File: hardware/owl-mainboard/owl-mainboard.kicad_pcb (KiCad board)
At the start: 4 copper layers, 61.8 x 79.8 mm, 107 parts, among them J101 Battery +, -, J201 USB-C, J202 EXP: GND, 3V3, A, B, J301 AMOLED FPC, J302 LRA, J303 DOCK: GND, VBUS, DET, GND, SW201 Ear left, SW202 Ear right, SW203 Beak, U101 BQ24073RGTR, U102 MAX17048G+T10, U103 TPS63802DLAR, U104 TPS22917DBVR, U201 ESP32-S3-WROOM-1-N16R8, U202 USBLC6-2SC6, U301 DRV2605LDGSR, U302 TMAG5273A2QDBVR, U303 LIS2DW12TR, U304 OPT3001DNPR, Y201 32.768kHz 12.5pF

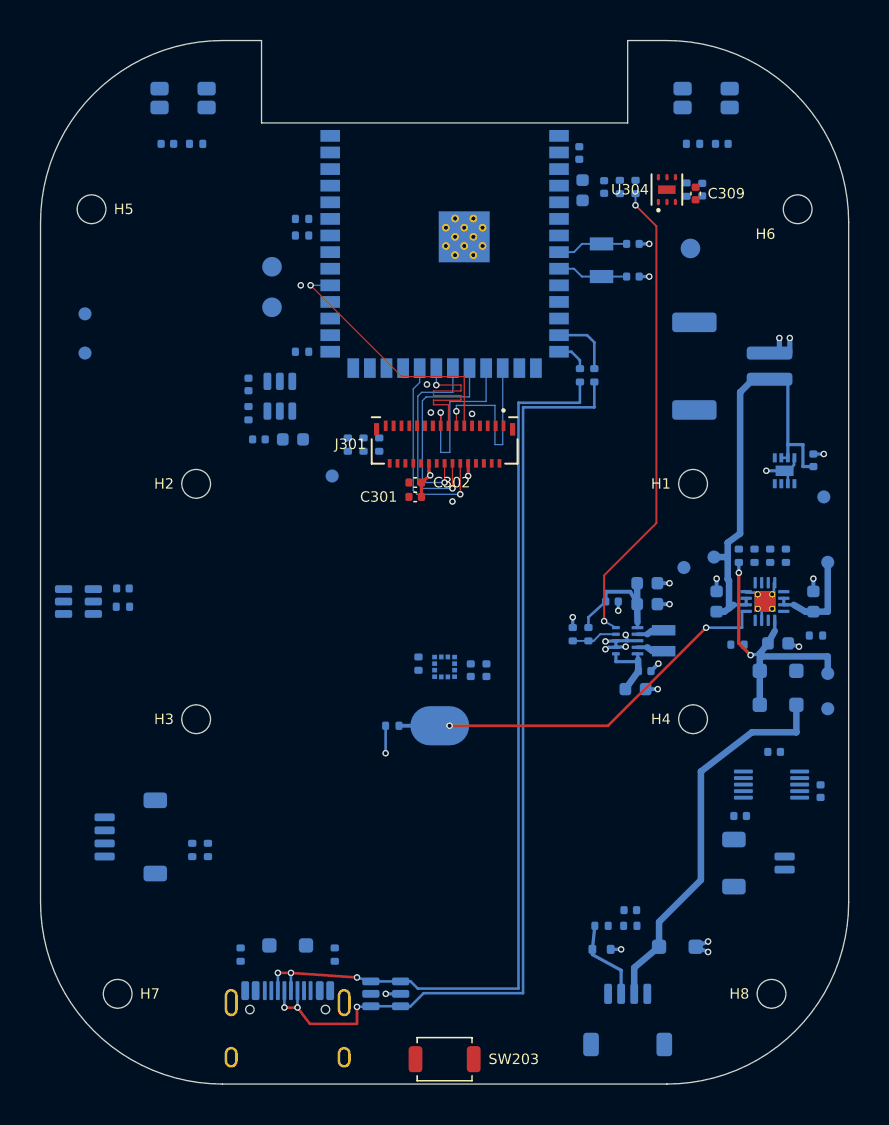
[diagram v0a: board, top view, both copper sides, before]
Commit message: feat(hardware): route VSYS to the TPS63802, the +3V3 feed to the module and VBUS_USB by hand
Three new hw_route.py groups, all 0.5 mm, locked and grouped, before
Freerouting takes the rest:

- vsys_link: the charger's VSYS copper is sealed in on B.Cu and In2 stays
  GND under U101, U103 and their caps, so VSYS crosses on F.Cu over In1:
  two vias at C105 (the bulk input cap), north between U103's west and
  channel GND vias, east between the channel and C109 vias, north west of
  the C107/C108 vias (clear of L101 and the switch pins), east at y 3.25,
  two vias on the charger's VSYS run. 30.0 mm.
- v3v3_feed: C108 to two vias west of the TPS_PG run, F.Cu up at x 7.0
  to two vias under the module (the In2 +3V3 pour goes there), and
  module pin 2 to two vias beside it. 25.9 mm.
- vbus_usb: both J201 VBUS pads into D201; the east pad hooks round R201
  so CC1 stays on B.Cu inside it and CC2 crosses on F.Cu; D201 and R201
  share two GND vias; F.Cu at y -24.55 and up the right side to two vias
  east of D101's anode. 73.3 mm.

DRC: no new violation type; VSYS, VBUS_USB, CC1 and CC2 are fully
connected (unconnected 216 to 209). The six new +3V3 and GND vias show
as via_dangling until the planes are poured.
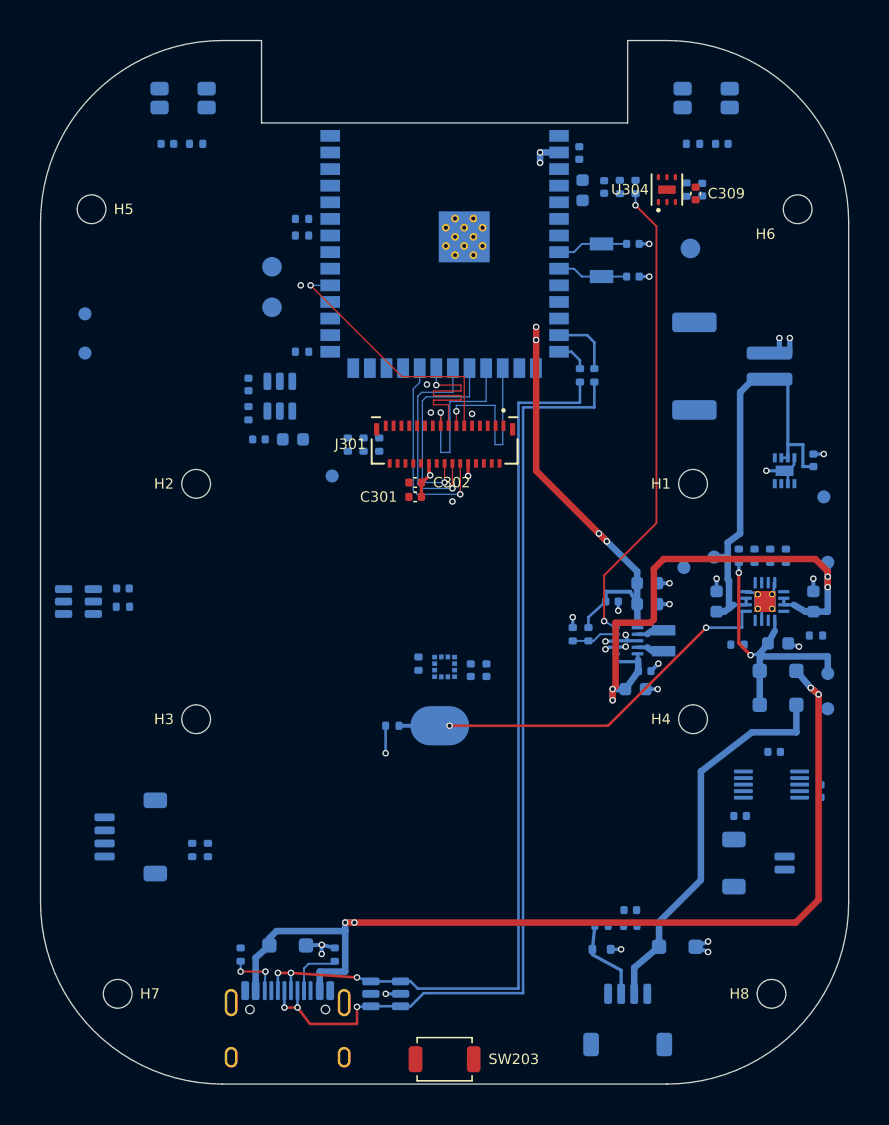
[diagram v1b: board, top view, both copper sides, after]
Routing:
- net VBUS_USB: track 0.00 -> 73.3 mm, vias 0 -> 4
- net VSYS: track 13.1 -> 43.1 mm, vias 0 -> 4
- net +3V3: track 9.69 -> 35.6 mm, vias 0 -> 6
- net USB_CC1: track 0.00 -> 3.74 mm
- net USB_CC2: track 0.00 -> 3.69 mm, vias 0 -> 2
- net GND: track 31.3 -> 34.2 mm, vias 31 -> 33

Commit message: feat(hardware): pour the In1 and In2 planes from hw_route.py
hw_route.py groups can now draw copper pours, (net, "pour", polygon,
layer, priority): 0.2 mm clearance, 0.2 mm minimum width, thermal reliefs
with a 0.3 mm gap and 0.3 mm spokes, islands removed, locked and in the
group's KiCad group, so a re-run replaces them; a run that draws a pour
refills every zone. A new test draws, fills and replaces pours on a
4-layer test board (it fails on the previous hw_route.py).

The planes group: In1 solid GND; In2 GND everywhere except a +3V3 pour
under the module inside its pin ring (x -8.4 to 8.4, y 18.8 up to the
antenna rule area at 36.6). The pour starts above the bottom pin row, so
the QSPI and USB stubs leaving the pins stay over GND, and Y201 keeps GND
under it. In2 is GND under U101, U103 and their caps, the crystal, the
QSPI block and the USB corridor. The In2 GND pour is notched round the
+3V3 pour, so the Specctra export gives Freerouting two planes that do
not overlap. RT101's In2 rule area and the antenna rule area clip the
fills.

DRC: every via_dangling is gone (all 37 GND and +3V3 vias reach a
plane); unconnected 209 to 176; no new violation type.
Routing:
- added copper zone on In2.Cu, net +3V3
- added copper zone on In1.Cu, net GND
- added copper zone on In2.Cu, net GND
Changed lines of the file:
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@@
+	)
+	(zone
+		(net "GND")
+		(locked yes)
+		(layer "In1.Cu")
+		(name "hw_route planes GND In1")
+		(hatch edge 0.5)
+		(connect_pads
+			(clearance 0.2)
+		)
+		(min_thickness 0.2)
+		(fill yes
+			(thermal_gap 0.3)
+			(thermal_bridge_width 0.3)
+			(island_removal_mode 0)
+		)
+		(polygon
+			(pts
+				(xy 68 138) (xy 132 138) (xy 132 56) (xy 68 56)
+			)
+		)
 	)
 	(zone
@@
 			(pts
 				(xy 97.38 108) (xy 101.88 108) (xy 101.88 111) (xy 97.38 111)
+			)
+		)
+	)
+	(zone
+		(net "GND")
+		(locked yes)
+		(layer "In2.Cu")
+		(name "hw_route planes GND In2")
+		(hatch edge 0.5)
+		(connect_pads
+			(clearance 0.2)
+		)
+		(min_thickness 0.2)
+		(fill yes
+			(thermal_gap 0.3)
+			(thermal_bridge_width 0.3)
+			(island_removal_mode 0)
+		)
+		(polygon
+			(pts
+				(xy 68 138) (xy 132 138) (xy 132 56) (xy 108.4 56) (xy 108.4 81.2) (xy 91.6 81.2) (xy 91.6 56) (xy 68 56)
+			)
+		)
+	)
+	(zone
+		(net "+3V3")
+		(locked yes)
+		(layer "In2.Cu")
+		(name "hw_route planes +3V3 In2")
+		(hatch edge 0.5)
+		(priority 1)
+		(connect_pads
+			(clearance 0.2)
+		)
+		(min_thickness 0.2)
+		(fill yes
+			(thermal_gap 0.3)
+			(thermal_bridge_width 0.3)
+			(island_removal_mode 0)
+		)
+		(polygon
+			(pts
+				(xy 91.6 81.2) (xy 108.4 81.2) (xy 108.4 63) (xy 91.6 63)
 			)
 		)
@@
 		)
 	)
+	(group "hw_route planes"
+		(members "35e60120-90ff-48d7-8a44-8b1ea687094f" "c799ce7a-62c5-46fe-9a01-1122aace69d0"
+			"d45afd2d-d90a-4230-a68f-48c74bce4e0a"
+		)
+	)

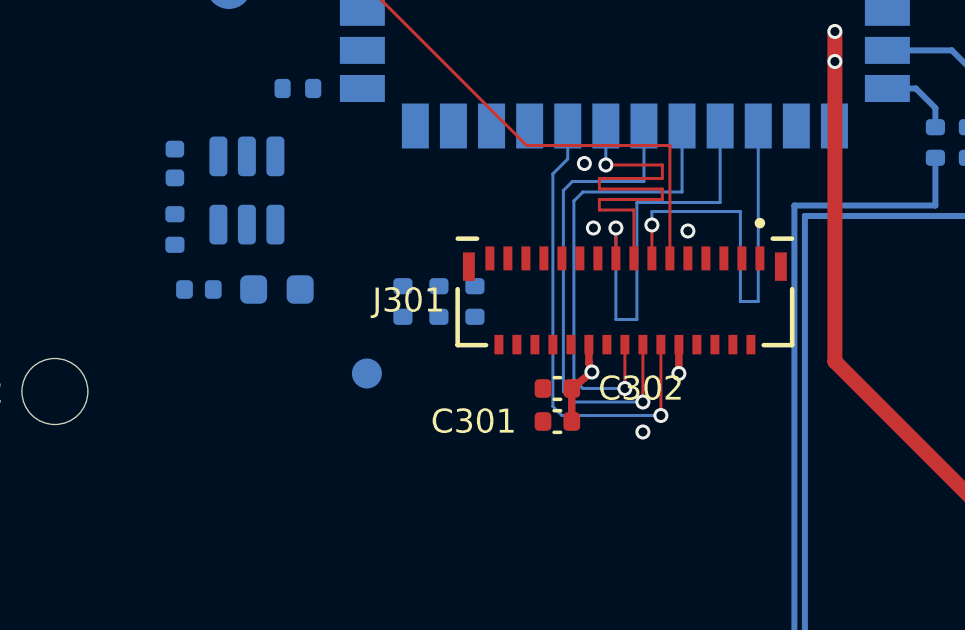
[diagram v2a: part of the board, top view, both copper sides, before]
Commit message: feat(hardware): keep routes from between J301's pads and route its fan-out and DISP_3V3 by hand
The first full Freerouting run put DISP_3V3, GND and LCD_RST tracks
between J301's two rows. hw_route.py gains ("", "keepout", polygon,
layer) rule areas (no tracks, vias or pours; pads allowed), and the qspi
group now draws one on F.Cu over the band between J301's rows and the
0.3 mm gaps between neighbouring pads (j301_comb). The Specctra export
hands it to Freerouting as a keepout. The rule-area test covers it.

New groups, locked and grouped:
- j301_fanout: every remaining J301 pin led out of the connector. Top
  row pins leave upwards to vias west of the B.Cu QSPI lanes (TP_SCL,
  TP_RST, GND 25, GND 31 with the west mounting pad), pin 1 joins the
  east mounting pad and a via, pin 7 the qspi GND via, pin 4 a via;
  TP_SDA, TP_INT and LCD_RST drop to vias below the bottom row.
- disp_3v3: the panel supply. The top row's DISP_3V3 pins reach the
  bottom row's through an F.Cu loop round the west end of J301 (0.3 mm)
  into C301 and C302; a via feeds the B.Cu side (R301 to R303, TP105,
  C111, C112, U104 pins 5 and 6) at 0.4 mm.

DRC: no clearance or keepout violation; the five signal vias wait for
Freerouting (via_dangling 5); unconnected 155.
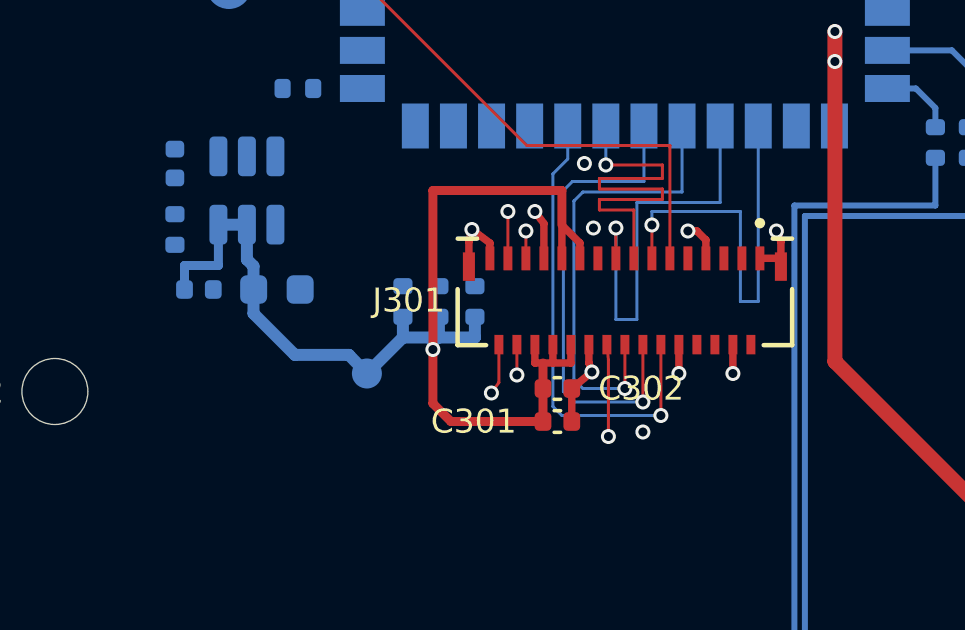
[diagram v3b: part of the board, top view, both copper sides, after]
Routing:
- net DISP_3V3: track 0.00 -> 42.4 mm, vias 0 -> 1
- net GND: track 34.2 -> 42.3 mm, vias 33 -> 37
- net LCD_RST: track 0.00 -> 3.06 mm, vias 0 -> 1
- net TP_INT: track 0.00 -> 1.69 mm, vias 0 -> 1
- net TP_RST: track 0.00 -> 1.56 mm, vias 0 -> 1
- net TP_SDA: track 0.00 -> 1.01 mm, vias 0 -> 1
- net TP_SCL: track 0.00 -> 0.91 mm, vias 0 -> 1

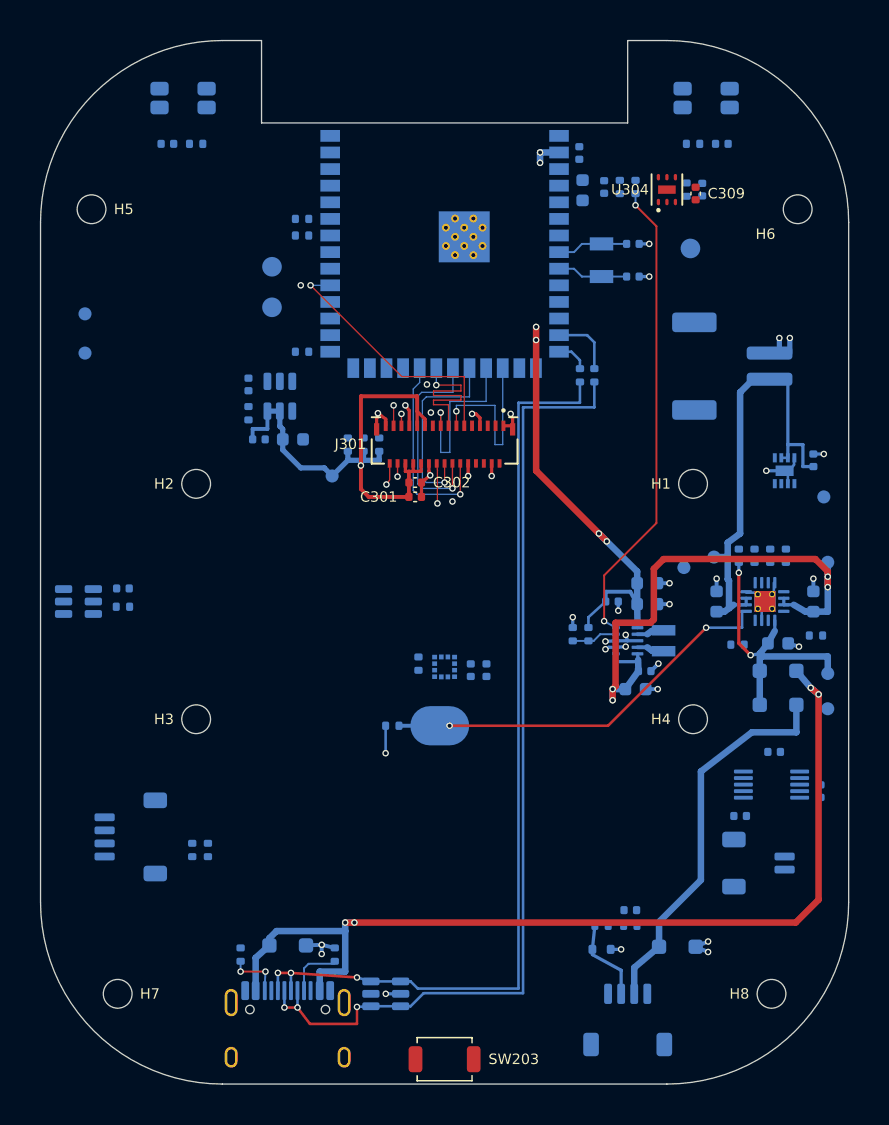
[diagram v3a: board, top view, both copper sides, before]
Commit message: feat(hardware): route the remaining main board nets with Freerouting
Freerouting 2.4.1 (Java 25, headless, analytics off) on KiCad's Specctra
export, prepared so that it routes only on F.Cu and B.Cu: In1 and In2
as power layers without the plane polygons (as signal layers it put
tracks on them; as power layers with the planes it fanned nothing out
to them; its autoroute_settings layer rules break the DSN load in
2.4.1), and the Power class at 0.25 mm since the 0.5 mm paths are hand
routed and fixed. Settings: -mp 40, via cost 30 (default 50) so nets
hop the 45 mm B.Cu USB pair with two vias (9 F.Cu crossings), hole
clearance 0.26 mm, copper to edge 0.32 mm, fan-out off. 254 items to
route, 70 left by Freerouting's count after 40 passes.

After the import every hw_route.py group was redrawn (the import adds
unlocked copies of locked copper) and 10 session echoes lying inside
locked tracks were deleted: 324 hand items, all locked and grouped;
79 routed vias, 679 mm on F.Cu and 1016 mm on B.Cu.

Checks: nothing enters the antenna rule area or J301's keep-out (DRC
has no items_not_allowed); under L101 only the session's 0.25 mm pad
entries into L101's own pads; under U302 only U302's own pins (its
3.3 V and GND, a few mA, no switching net).

DRC: 19 unconnected (+3V3 9 and GND 6 at U303, U301 and C304 where
the 0.5 mm pitch pins defeat the 0.2 mm Power clearance, 2 GND tracks,
LCD_RST, I2C_SDA), 3 hole_clearance near J301 and the module's west
column, 1 dangling LCD_RST via; fixed by hand next.
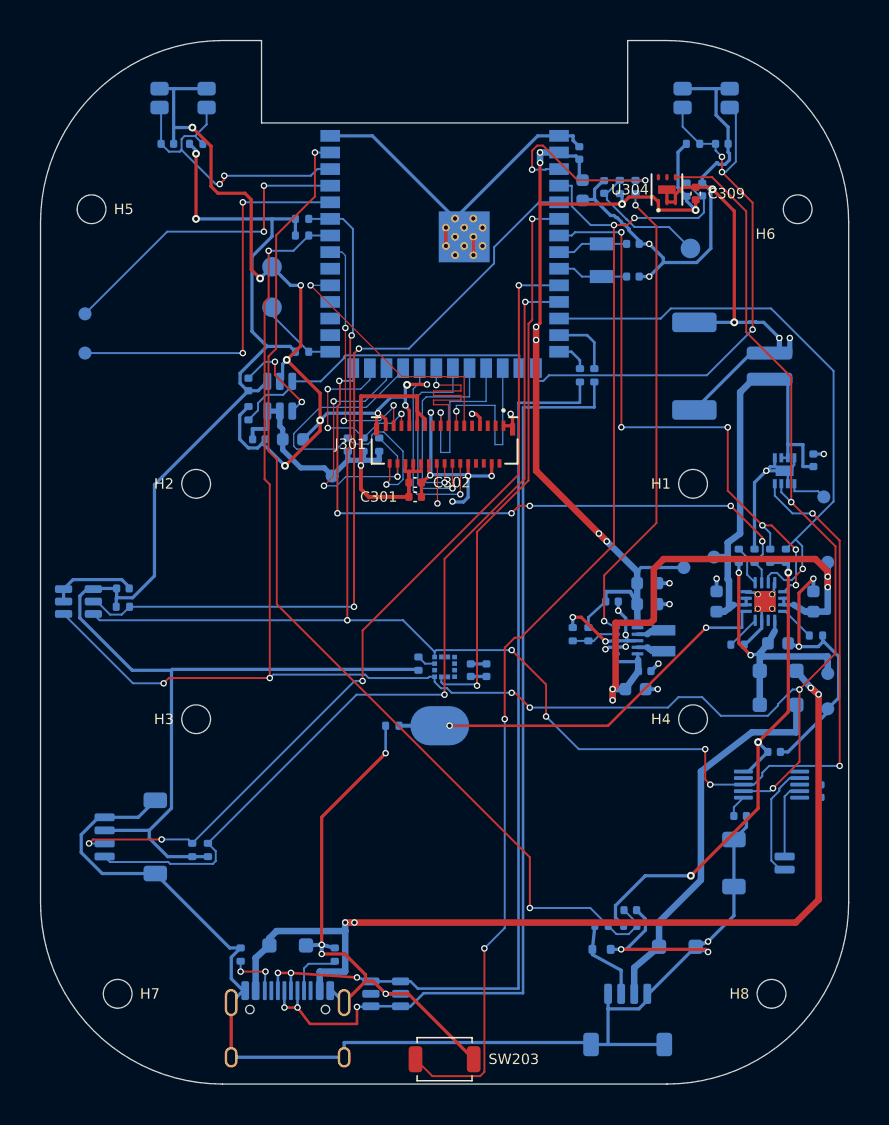
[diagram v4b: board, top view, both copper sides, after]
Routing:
- net GND: track 42.3 -> 411.4 mm, vias 37 -> 45
- net +3V3: track 35.6 -> 228.3 mm, vias 6 -> 13
- net I2C_SCL: track 0.00 -> 159.6 mm, vias 0 -> 8
- net I2C_SDA: track 0.00 -> 124.9 mm, vias 0 -> 8
- net BTN_BEAK: track 0.00 -> 91.7 mm, vias 0 -> 4
- net DOCK_DET: track 0.00 -> 79.6 mm, vias 0 -> 2
- net EXP_B: track 0.00 -> 68.4 mm, vias 0 -> 2
- net EXP_A: track 0.00 -> 65.8 mm, vias 0 -> 4
- net HALL_INT: track 0.00 -> 61.2 mm, vias 0 -> 2
- net CHG_SUSPEND: track 0.00 -> 50.0 mm, vias 0 -> 6
- net CHG_PGOOD: track 0.00 -> 47.0 mm, vias 0 -> 5
- net BTN_EAR_R: track 0.00 -> 44.8 mm, vias 0 -> 3
- net CHG_STAT: track 0.00 -> 43.5 mm, vias 0 -> 2
- net IMU_INT1: track 0.00 -> 42.7 mm, vias 0 -> 2
- net U0RXD: track 0.00 -> 30.3 mm, vias 0 -> 2
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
